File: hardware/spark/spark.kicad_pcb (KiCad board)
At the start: 2 copper layers, 16 parts, among them J1 Conn_01x05_Pin, J2 Conn_01x02, Q1 STD2805T4, Q2 PMBT2369

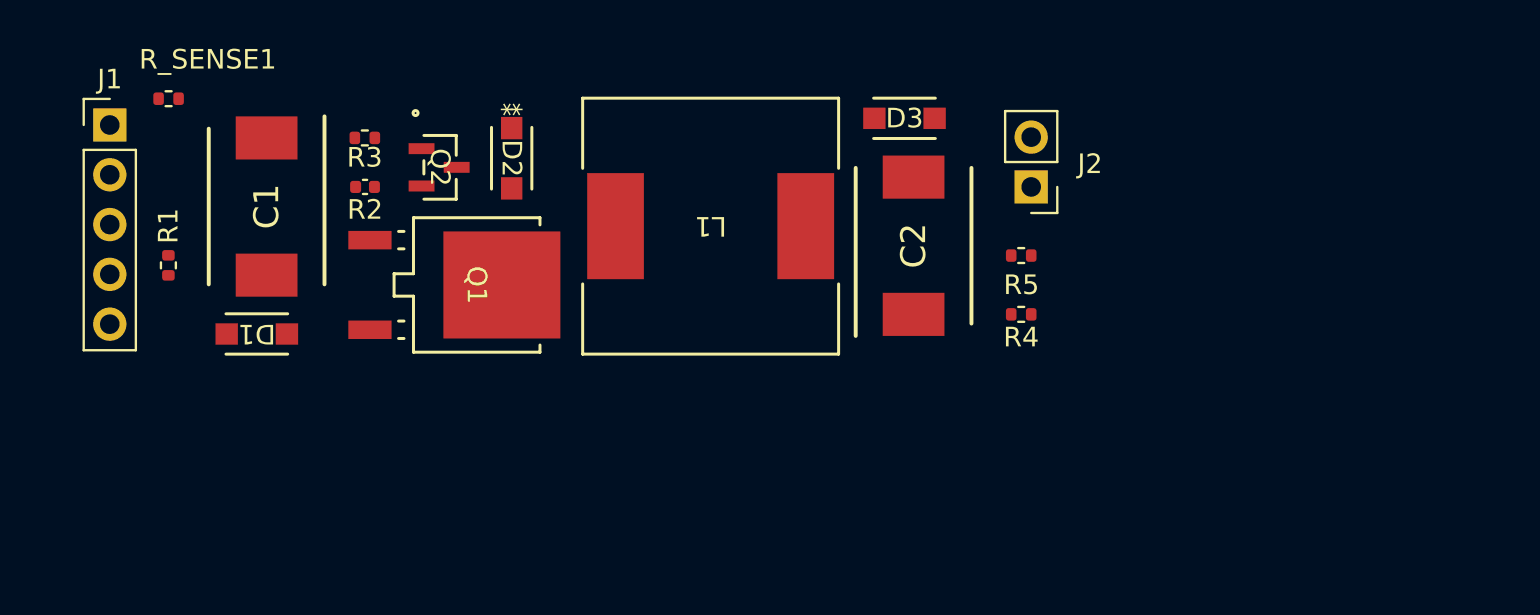
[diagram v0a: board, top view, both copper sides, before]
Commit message: First pass routing of traces
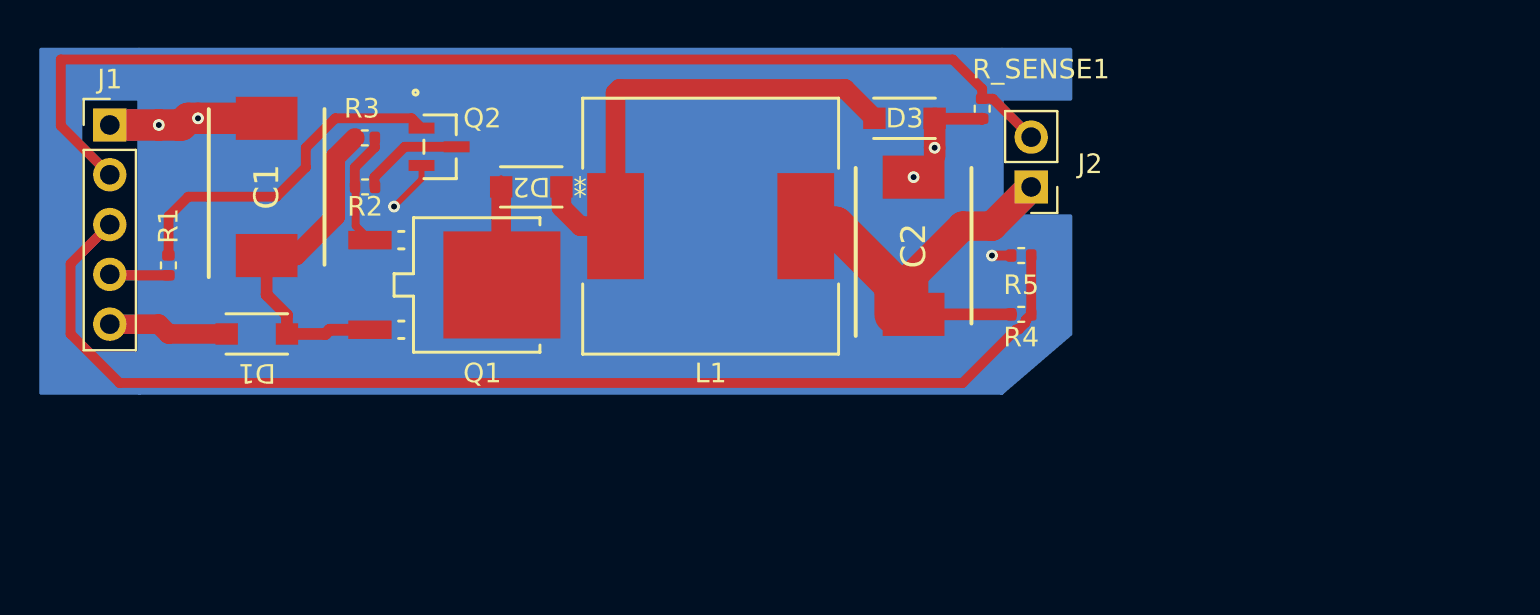
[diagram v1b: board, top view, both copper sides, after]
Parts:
- R2: footprint Capacitor_SMD:C_0402_1005Metric -> Resistor_SMD:R_0402_1005Metric
- moved R_SENSE1 41.5 mm to (149.5, 85.0), turned to 90 degrees
- moved D2 1.77 mm to (126.5, 89.0), turned to 180 degrees
- moved Q2 1.05 mm to (121.8, 87.0)
- moved C1 1.00 mm to (113.0, 89.0), turned to 90 degrees
- turned R2 to 0 degrees
- turned R5 to 0 degrees
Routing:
- net /V_SENSE: track 0.00 -> 61.0 mm
- net /I_SENSE: track 0.00 -> 58.9 mm
- net Net-(D2-Pad1): track 0.00 -> 24.9 mm
- net Net-(J2-Pin_1): track 0.00 -> 23.1 mm
- net Net-(C1-Pad1): track 0.00 -> 17.8 mm
- net Net-(Q2-Pad1): track 0.00 -> 17.8 mm
- net GND: track 0.00 -> 17.7 mm, vias 0 -> 6
- net Net-(Q1-Pad1): track 0.00 -> 6.31 mm
- net /+5V: track 0.00 -> 6.17 mm
- net Net-(D2-Pad2): track 0.00 -> 5.77 mm
- net Net-(Q2-Pad3): track 0.00 -> 5.34 mm
- net /PWM: track 0.00 -> 3.01 mm

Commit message: Cleanup
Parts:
- moved L1 21.3 mm to (154.9, 100.3)
- moved R1 21.3 mm to (127.2, 102.3)
- moved R2 21.3 mm to (137.2, 98.3)
- moved C1 21.3 mm to (132.2, 98.3)
- moved C2 21.3 mm to (165.2, 101.3)
- moved D1 21.3 mm to (131.7, 105.8)
- moved D2 21.3 mm to (145.7, 98.3)
- moved D3 21.3 mm to (164.7, 94.8)
- moved J1 21.3 mm to (124.2, 95.1)
- moved J2 21.3 mm to (171.2, 98.3)
- moved Q1 21.3 mm to (142.9, 103.3)
- moved Q2 21.3 mm to (141.1, 96.2)
- moved R4 21.3 mm to (170.7, 104.8)
- moved R5 21.3 mm to (170.7, 101.8)
- moved R_SENSE1 21.3 mm to (168.7, 94.3)
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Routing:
- net /V_SENSE: track 61.0 -> 62.3 mm
